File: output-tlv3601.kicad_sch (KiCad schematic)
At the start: 8 parts, among them J3 SMA, U31 TLV3601DCKR

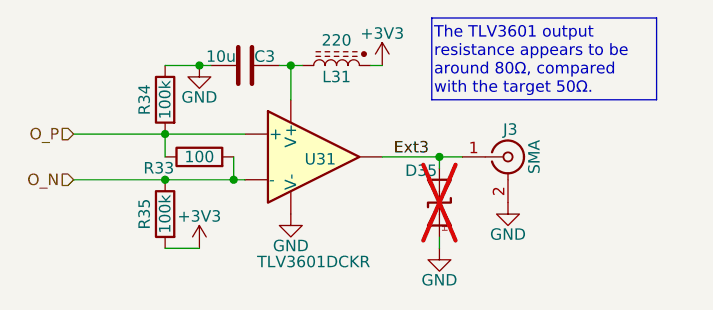
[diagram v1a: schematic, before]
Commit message: FPGA in, layout mostly updated.
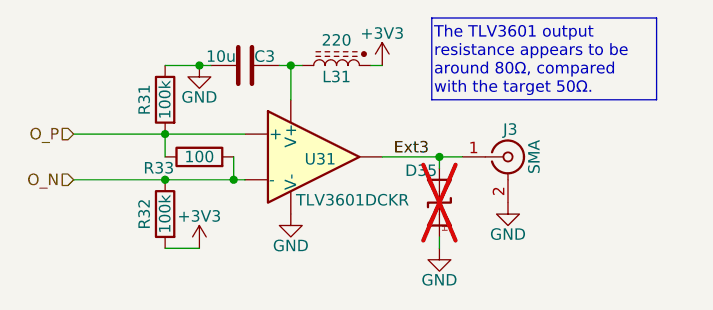
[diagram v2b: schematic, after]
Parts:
- renumbered R34 to R31, R35 to R32
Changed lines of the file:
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@@
-					(unit 1)
-				)
-				(path "/3160ff17-81c2-4674-af97-e8d9acaf6b65/d9ae02c3-f798-426e-9122-f6e2522738d6"
-					(reference "#PWR042")
 					(unit 1)
 				)
@@
 		(in_pos_files yes)
 		(dnp no)
-		(property "Reference" "R34"
+		(property "Reference" "R31"
 			(at 58.674 107.95 90)
 			(show_name no)
@@
 			(project "gpsfreak"
 				(path "/3160ff17-81c2-4674-af97-e8d9acaf6b65/bc4a3f50-85d7-4b0d-bb14-10533109d674"
-					(reference "R34")
-					(unit 1)
-				)
-				(path "/3160ff17-81c2-4674-af97-e8d9acaf6b65/d9ae02c3-f798-426e-9122-f6e2522738d6"
-					(reference "R37")
+					(reference "R31")
 					(unit 1)
 				)
@@
 					(unit 1)
 				)
-				(path "/3160ff17-81c2-4674-af97-e8d9acaf6b65/d9ae02c3-f798-426e-9122-f6e2522738d6"
-					(reference "D36")
-					(unit 1)
-				)
 			)
 		)
@@
 		(in_pos_files yes)
 		(dnp no)
-		(property "Reference" "R35"
+		(property "Reference" "R32"
 			(at 58.674 120.65 90)
 			(show_name no)
@@
 			(project "gpsfreak"
 				(path "/3160ff17-81c2-4674-af97-e8d9acaf6b65/bc4a3f50-85d7-4b0d-bb14-10533109d674"
-					(reference "R35")
-					(unit 1)
-				)
-				(path "/3160ff17-81c2-4674-af97-e8d9acaf6b65/d9ae02c3-f798-426e-9122-f6e2522738d6"
-					(reference "R38")
+					(reference "R32")
 					(unit 1)
 				)
@@
 					(unit 1)
 				)
-				(path "/3160ff17-81c2-4674-af97-e8d9acaf6b65/d9ae02c3-f798-426e-9122-f6e2522738d6"
-					(reference "R36")
-					(unit 1)
-				)
 			)
 		)
@@
 					(unit 1)
 				)
-				(path "/3160ff17-81c2-4674-af97-e8d9acaf6b65/d9ae02c3-f798-426e-9122-f6e2522738d6"
-					(reference "J4")
-					(unit 1)
-				)
 			)
 		)
@@
 				(path "/3160ff17-81c2-4674-af97-e8d9acaf6b65/bc4a3f50-85d7-4b0d-bb14-10533109d674"
 					(reference "#PWR038")
-					(unit 1)
-				)
-				(path "/3160ff17-81c2-4674-af97-e8d9acaf6b65/d9ae02c3-f798-426e-9122-f6e2522738d6"
-					(reference "#PWR043")
 					(unit 1)
 				)
@@
 					(unit 1)
 				)
-				(path "/3160ff17-81c2-4674-af97-e8d9acaf6b65/d9ae02c3-f798-426e-9122-f6e2522738d6"
-					(reference "L32")
-					(unit 1)
-				)
 			)
 		)
@@
 					(unit 1)
 				)
-				(path "/3160ff17-81c2-4674-af97-e8d9acaf6b65/d9ae02c3-f798-426e-9122-f6e2522738d6"
-					(reference "#PWR048")
-					(unit 1)
-				)
 			)
 		)
@@
 					(unit 1)
 				)
-				(path "/3160ff17-81c2-4674-af97-e8d9acaf6b65/d9ae02c3-f798-426e-9122-f6e2522738d6"
-					(reference "#PWR052")
-					(unit 1)
-				)
 			)
 		)
@@
 				(path "/3160ff17-81c2-4674-af97-e8d9acaf6b65/bc4a3f50-85d7-4b0d-bb14-10533109d674"
 					(reference "#PWR050")
-					(unit 1)
-				)
-				(path "/3160ff17-81c2-4674-af97-e8d9acaf6b65/d9ae02c3-f798-426e-9122-f6e2522738d6"
-					(reference "#PWR054")
 					(unit 1)
 				)
@@
 					(unit 1)
 				)
-				(path "/3160ff17-81c2-4674-af97-e8d9acaf6b65/d9ae02c3-f798-426e-9122-f6e2522738d6"
-					(reference "C39")
-					(unit 1)
-				)
 			)
 		)
@@
 					(unit 1)
 				)
-				(path "/3160ff17-81c2-4674-af97-e8d9acaf6b65/d9ae02c3-f798-426e-9122-f6e2522738d6"
-					(reference "#PWR051")
-					(unit 1)
-				)
 			)
 		)
@@
 		)
 		(property "Value" "TLV3601DCKR"
-			(at 77.47 125.222 0)
+			(at 81.788 118.364 0)
 			(show_name no)
 			(do_not_autoplace no)
@@
 					(unit 1)
 				)
-				(path "/3160ff17-81c2-4674-af97-e8d9acaf6b65/d9ae02c3-f798-426e-9122-f6e2522738d6"
-					(reference "U32")
-					(unit 1)
-				)

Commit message: Layout down
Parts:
- C3, R31, R32, R33: Stock (none) -> Basic
- D35: Stock (none) -> N/A
- J3: Stock (none) -> AliX
- L31: value 220 -> 120; Stock (none) -> Basic
- U31: Stock (none) -> Ext
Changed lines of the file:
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@@
+			)
+		)
+		(property "Stock" "Basic"
+			(at 60.96 107.95 90)
+			(hide yes)
+			(show_name no)
+			(do_not_autoplace no)
+			(effects
+				(font
+					(size 1.27 1.27)
+				)
 			)
 		)
@@
 			)
 		)
+		(property "Stock" "N/A"
+			(at 91.44 119.38 90)
+			(hide yes)
+			(show_name no)
+			(do_not_autoplace no)
+			(effects
+				(font
+					(size 1.27 1.27)
+				)
+			)
+		)
 		(pin "2"
 		)
@@
 			)
 		)
+		(property "Stock" "Basic"
+			(at 60.96 120.65 90)
+			(hide yes)
+			(show_name no)
+			(do_not_autoplace no)
+			(effects
+				(font
+					(size 1.27 1.27)
+				)
+			)
+		)
 		(pin "2"
 		)
@@
 			)
 		)
+		(property "Stock" "Basic"
+			(at 64.77 114.3 90)
+			(hide yes)
+			(show_name no)
+			(do_not_autoplace no)
+			(effects
+				(font
+					(size 1.27 1.27)
+				)
+			)
+		)
 		(pin "2"
 		)
@@
 			)
 		)
+		(property "Stock" "AliX"
+			(at 99.06 114.3 0)
+			(hide yes)
+			(show_name no)
+			(do_not_autoplace no)
+			(effects
+				(font
+					(size 1.27 1.27)
+				)
+			)
+		)
 		(pin "2"
 		)
@@
 			)
 		)
-		(property "Value" "220"
+		(property "Value" "120"
 			(at 80.01 101.346 90)
 			(show_name no)
@@
 		)
 		(property "LCSC" "C14709"
+			(at 80.01 104.14 90)
+			(hide yes)
+			(show_name no)
+			(do_not_autoplace no)
+			(effects
+				(font
+					(size 1.27 1.27)
+				)
+			)
+		)
+		(property "Stock" "Basic"
 			(at 80.01 104.14 90)
 			(hide yes)
@@
 			)
 		)
+		(property "Stock" "Basic"
+			(at 69.85 104.14 90)
+			(hide yes)
+			(show_name no)
+			(do_not_autoplace no)
+			(effects
+				(font
+					(size 1.27 1.27)
+				)
+			)
+		)
 		(pin "1"
 		)
@@
 			(at 77.47 114.3 0)
 			(hide yes)
+			(show_name no)
+			(do_not_autoplace no)
+			(effects
+				(font
+					(size 1.27 1.27)
+				)
+			)
+		)
+		(property "Stock" "Ext"
+			(at 77.47 114.3 0)
+			(hide yes)

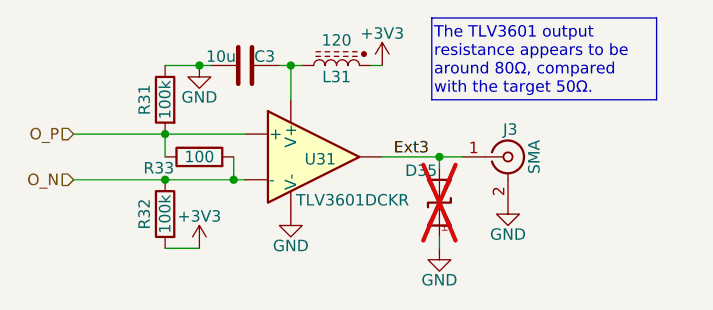
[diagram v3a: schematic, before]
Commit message: Adjustments.  Silk screen clearance.
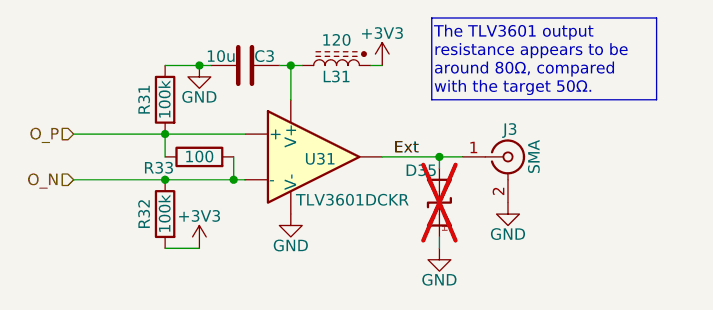
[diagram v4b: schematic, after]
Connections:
- net Ext3 renamed Ext
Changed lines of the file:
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@@
 		)
 	)
-	(label "Ext3"
+	(label "Ext"
 		(at 86.36 114.3 0)
 		(effects

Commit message: Change the 10µF 0402 part number.
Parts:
- C3: LCSC C15525 -> C315248; Stock Basic -> Ext
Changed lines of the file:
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@@
 			)
 		)
-		(property "Datasheet" ""
+		(property "Datasheet" "10V"
 			(at 69.85 104.14 0)
 			(hide yes)
@@
 			)
 		)
-		(property "LCSC" "C15525"
+		(property "LCSC" "C315248"
 			(at 69.85 104.14 0)
 			(hide yes)
@@
 			)
 		)
-		(property "Stock" "Basic"
+		(property "Stock" "Ext"
 			(at 69.85 104.14 90)
 			(hide yes)
